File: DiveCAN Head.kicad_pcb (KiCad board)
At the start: 4 copper layers, 55 x 41.8 mm, 114 parts, among them J1 Cell 1, J10 SOLENOID OUT, J2 Cell 2, J3 Cell 3, J4 POWER CONNECTION, J5 SSC1, J6 SSC1, J7 SSC1, J8 Conn_01x05_Socket, J9 Conn_01x05_Socket, Q2 DMG1012T, U1 ATtiny102-SS, U10 AVR32EA28, U11 MCP2515-xSO, U12 TCAN330, U13 TPS63001, U15 74LVC2G14, U16 TPS63001, U2 TPS2115, U3 ATtiny102-SS, U4 TPS2115, U5 ATtiny102-SS, U6 TPS2115, U7 AVR32EA28, U8 MCP2515-xSO, U9 TCAN330

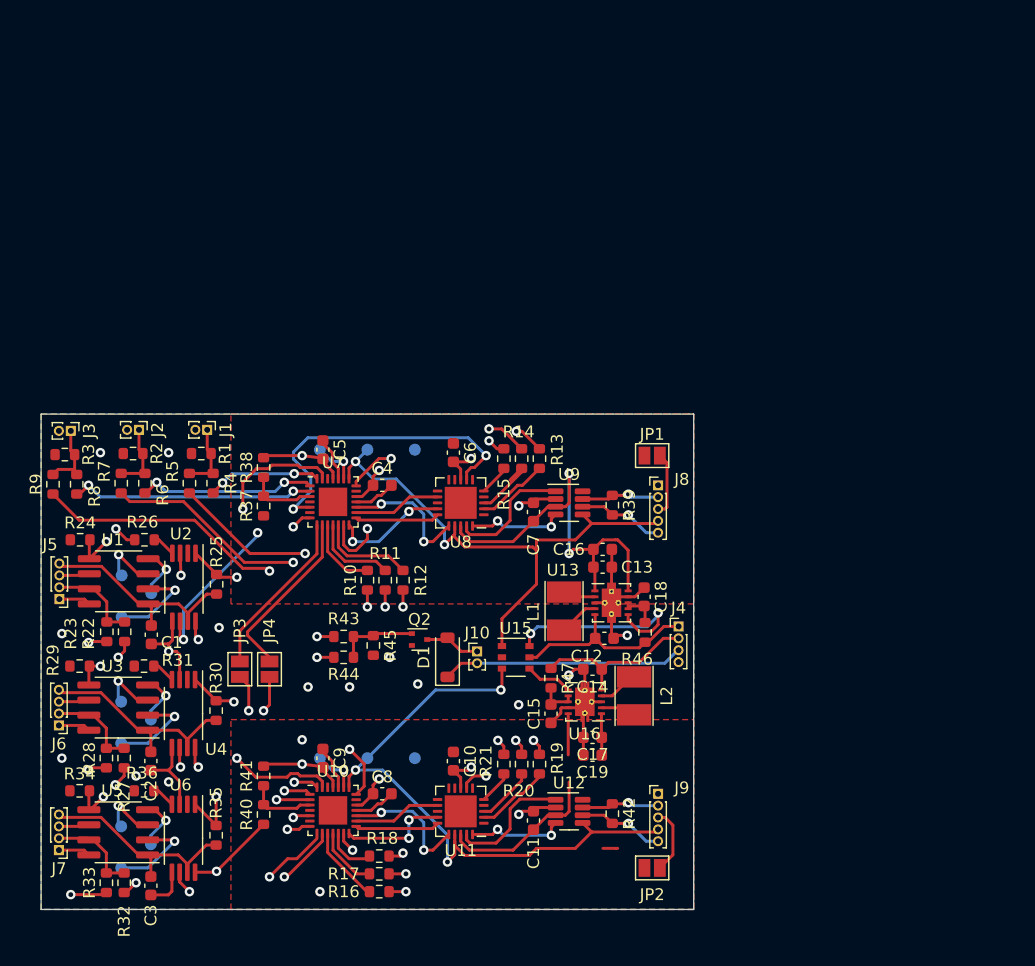
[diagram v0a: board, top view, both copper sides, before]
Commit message: 
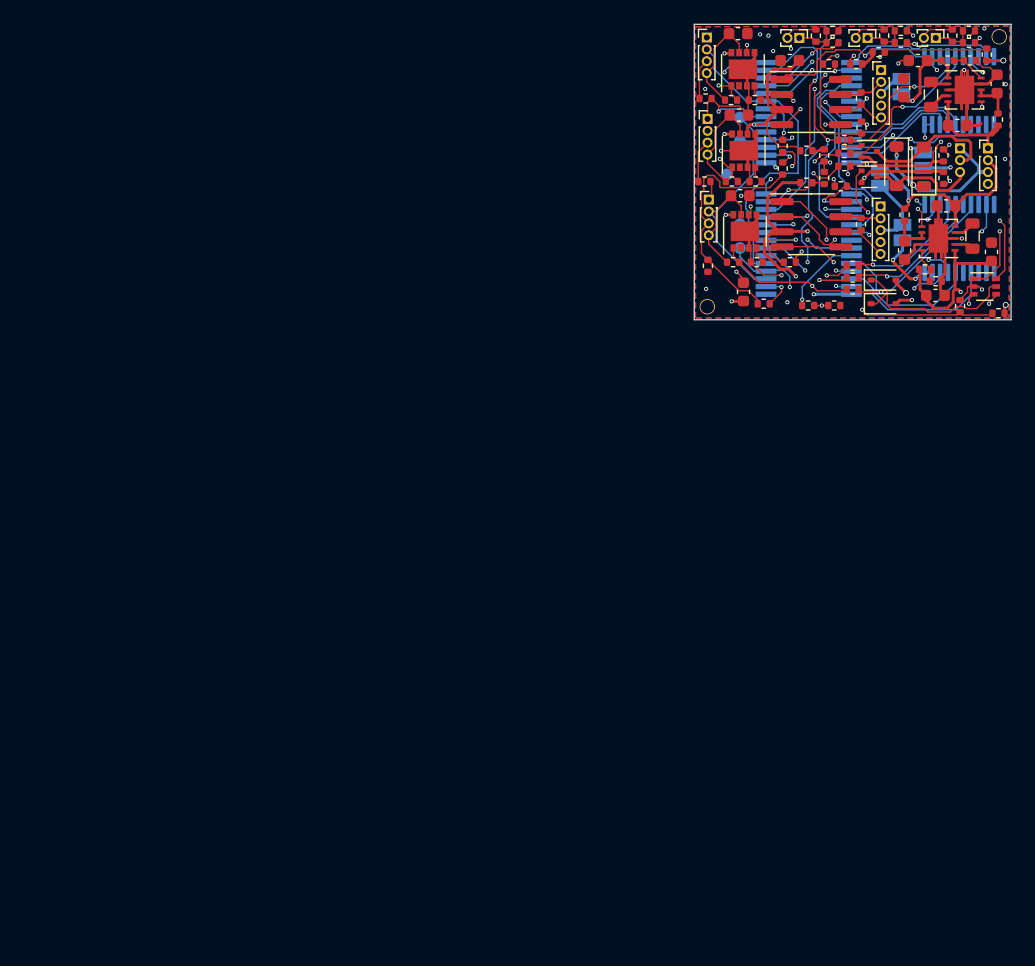
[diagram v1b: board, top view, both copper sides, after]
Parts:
- removed the C10 at (79.8, 154.2)
- removed the C11 at (86.5, 159.2)
- removed the C5 at (68.8, 128.0)
- removed the C6 at (79.8, 128.2)
- removed the C7 at (86.5, 133.2)
- removed the C9 at (68.8, 154.0)
- removed the J1 at (59.0, 126.3)
- removed the J3 at (47.5, 126.4)
- removed the R24 at (48.3, 135.6)
- removed the R27 at (52.0, 154.0)
- removed the R28 at (50.5, 154.0)
- removed the R29 at (48.2, 146.2)
- removed the R34 at (48.2, 156.8)
- removed the R4 at (59.5, 130.8)
- removed the R5 at (57.5, 130.8)
- removed the R6 at (53.8, 130.8)
- removed the R7 at (51.8, 130.8)
- removed the R8 at (48.0, 130.9)
- removed the R9 at (46.0, 130.9)
- removed TP12, TP15: GND, TestPoint:TestPoint_Pad_D1.0mm
- removed the TP2 at (51.8, 138.6)
- removed the TP3 at (51.8, 142.1)
- removed the TP4 at (54.2, 150.7)
- removed the TP5 at (51.8, 149.2)
- removed TP6, TP9: SSC_TPICLK, TestPoint:TestPoint_Pad_D1.0mm
- removed TP7: SSC_RST, TestPoint:TestPoint_Pad_D1.0mm
- removed TP8: SSC_TPIDATA, TestPoint:TestPoint_Pad_D1.0mm
- removed the U1 at (51.5, 139.1)
- removed the U3 at (51.5, 149.7)
- removed the U5 at (51.5, 160.2)
- added D1: 1N5819WS, Diode_SMD:D_SOD-323, F.Cu at (116.0, 113.7)
- added D2: 1N5819WS, Diode_SMD:D_SOD-323, F.Cu at (116.0, 115.7)
- added D3: MBR0520, Diode_SMD:D_SOD-123, F.Cu at (119.4, 104.2)
- added J8: C1, Library:PinHeader_1x02_P1.00mm_Vertical, F.Cu at (120.4, 93.3)
- added J9: C1, Library:PinHeader_1x02_P1.00mm_Vertical, F.Cu at (114.7, 93.3)
- added Q1: DMG1012T, Package_TO_SOT_SMD:SOT-523, F.Cu at (114.8, 102.8)
- added R12: 200, Resistor_SMD:R_0402_1005Metric, F.Cu at (114.2, 100.8)
- added R13: 1M, Resistor_SMD:R_0402_1005Metric, F.Cu at (113.7, 95.5)
- added R20: 0.5, Resistor_SMD:R_0402_1005Metric, F.Cu at (121.0, 103.2)
- added R21: 200, Resistor_SMD:R_0402_1005Metric, F.Cu at (109.7, 115.8)
- added R37: 4.02k, Resistor_SMD:R_0402_1005Metric, F.Cu at (122.5, 115.9)
- added R38: 499k, Resistor_SMD:R_0402_1005Metric, F.Cu at (125.7, 116.5)
- added R40: 10K, Resistor_SMD:R_0402_1005Metric, F.Cu at (121.8, 93.1)
- added R41: 10K, Resistor_SMD:R_0402_1005Metric, F.Cu at (123.2, 93.7)
- added R42: 10K, Resistor_SMD:R_0402_1005Metric, F.Cu at (123.2, 92.7)
- added R46: 10K, Resistor_SMD:R_0402_1005Metric, F.Cu at (110.3, 93.1)
- added R47: 10K, Resistor_SMD:R_0402_1005Metric, F.Cu at (111.7, 93.7)
- added R48: 10K, Resistor_SMD:R_0402_1005Metric, F.Cu at (111.7, 92.7)
- added R49: 1M, Resistor_SMD:R_0402_1005Metric, F.Cu at (119.5, 112.8)
- added R50: 178k, Resistor_SMD:R_0402_1005Metric, F.Cu at (120.4, 113.8)
- added R51: 1M, Resistor_SMD:R_0402_1005Metric, F.Cu at (121.4, 95.2)
- added R52: 178k, Resistor_SMD:R_0402_1005Metric, F.Cu at (123.3, 95.2)
- added REF**: ToolingHoleJLC, Library:ToolingHoleJLC, F.Cu at (101.2, 116.0)
- added REF**: ToolingHoleJLC, Library:ToolingHoleJLC, F.Cu at (125.8, 93.2)
- J10: value SOLENOID OUT -> C1; footprint Connector_PinHeader_1.00mm:PinHeader_1x02_P1.00mm_Vertical -> Library:PinHeader_1x02_P1.00mm_Vertical
- J2: value Cell 2 -> Solenoid out; footprint Connector_PinHeader_1.00mm:PinHeader_1x02_P1.00mm_Vertical -> Connector_PinHeader_1.00mm:PinHeader_1x03_P1.00mm_Vertical; moved to B.Cu
- JP1, JP2, JP3, JP4: moved to B.Cu
- L1: renamed from L2; footprint Inductor_SMD:L_Taiyo-Yuden_NR-30xx_HandSoldering -> Inductor_SMD:L_0805_2012Metric
- L2: renamed from L1; footprint Inductor_SMD:L_Taiyo-Yuden_NR-30xx_HandSoldering -> Inductor_SMD:L_0805_2012Metric
- R1, R2, R3: value 10K -> 100k; footprint Resistor_SMD:R_0603_1608Metric -> Resistor_SMD:R_0402_1005Metric
- R10: renamed from R14; footprint Resistor_SMD:R_0603_1608Metric -> Resistor_SMD:R_0402_1005Metric
- R11: renamed from R15; footprint Resistor_SMD:R_0603_1608Metric -> Resistor_SMD:R_0402_1005Metric
- R14: renamed from R16; footprint Resistor_SMD:R_0603_1608Metric -> Resistor_SMD:R_0402_1005Metric
- R15: renamed from R17; footprint Resistor_SMD:R_0603_1608Metric -> Resistor_SMD:R_0402_1005Metric
- R16: renamed from R18; footprint Resistor_SMD:R_0603_1608Metric -> Resistor_SMD:R_0402_1005Metric
- R17: renamed from R19; footprint Resistor_SMD:R_0603_1608Metric -> Resistor_SMD:R_0402_1005Metric
- R18: renamed from R20; footprint Resistor_SMD:R_0603_1608Metric -> Resistor_SMD:R_0402_1005Metric
- R19: renamed from R21; footprint Resistor_SMD:R_0603_1608Metric -> Resistor_SMD:R_0402_1005Metric
- R22: value 5K -> 1M; footprint Resistor_SMD:R_0603_1608Metric -> Resistor_SMD:R_0402_1005Metric
- R23: value 5K -> 0.5; footprint Resistor_SMD:R_0603_1608Metric -> Resistor_SMD:R_0402_1005Metric
- R24: renamed from R25; footprint Resistor_SMD:R_0603_1608Metric -> Resistor_SMD:R_0402_1005Metric
- R25: renamed from R26; footprint Resistor_SMD:R_0603_1608Metric -> Resistor_SMD:R_0402_1005Metric
- R26: renamed from R30; footprint Resistor_SMD:R_0603_1608Metric -> Resistor_SMD:R_0402_1005Metric
- R27: renamed from R31; footprint Resistor_SMD:R_0603_1608Metric -> Resistor_SMD:R_0402_1005Metric
- R28: renamed from R35; footprint Resistor_SMD:R_0603_1608Metric -> Resistor_SMD:R_0402_1005Metric
- R29: renamed from R36; footprint Resistor_SMD:R_0603_1608Metric -> Resistor_SMD:R_0402_1005Metric
- R30: renamed from R37; value R -> 100k; footprint Resistor_SMD:R_0603_1608Metric -> Resistor_SMD:R_0402_1005Metric
- R31: renamed from R38; value R -> 4k; footprint Resistor_SMD:R_0603_1608Metric -> Resistor_SMD:R_0402_1005Metric
- R32: value 5K -> 4.02k; footprint Resistor_SMD:R_0603_1608Metric -> Resistor_SMD:R_0402_1005Metric
- R33: value 5K -> 499k; footprint Resistor_SMD:R_0603_1608Metric -> Resistor_SMD:R_0402_1005Metric
- R34: renamed from R39; footprint Resistor_SMD:R_0603_1608Metric -> Resistor_SMD:R_0402_1005Metric
- R35: renamed from R40; value R -> 100k; footprint Resistor_SMD:R_0603_1608Metric -> Resistor_SMD:R_0402_1005Metric
- R36: renamed from R41; value R -> 4k; footprint Resistor_SMD:R_0603_1608Metric -> Resistor_SMD:R_0402_1005Metric
- R39: renamed from R42; footprint Resistor_SMD:R_0603_1608Metric -> Resistor_SMD:R_0402_1005Metric
- R4: renamed from R47; footprint Resistor_SMD:R_0603_1608Metric -> Resistor_SMD:R_0402_1005Metric
- R43, R44: value 5K -> 10K; footprint Resistor_SMD:R_0603_1608Metric -> Resistor_SMD:R_0402_1005Metric
- R45: value 20K -> 10K; footprint Resistor_SMD:R_0603_1608Metric -> Resistor_SMD:R_0402_1005Metric
- R5: renamed from R46; footprint Resistor_SMD:R_0603_1608Metric -> Resistor_SMD:R_0402_1005Metric
- R6: renamed from R10; footprint Resistor_SMD:R_0603_1608Metric -> Resistor_SMD:R_0402_1005Metric
- R7: renamed from R11; footprint Resistor_SMD:R_0603_1608Metric -> Resistor_SMD:R_0402_1005Metric
- R8: renamed from R12; footprint Resistor_SMD:R_0603_1608Metric -> Resistor_SMD:R_0402_1005Metric
- R9: renamed from R13; footprint Resistor_SMD:R_0603_1608Metric -> Resistor_SMD:R_0402_1005Metric
- TP1: value SSC_RST -> GND
- U1: renamed from U15; footprint Package_SO:TSOP-6_1.65x3.05mm_P0.95mm -> Package_TO_SOT_SMD:SOT-363_SC-70-6
- U10, U7: footprint Package_DFN_QFN:VQFN-28-1EP_4x4mm_P0.45mm_EP2.4x2.4mm -> Package_SO:SSOP-28_5.3x10.2mm_P0.65mm; moved to B.Cu
- U11, U8: footprint Package_DFN_QFN:QFN-20-1EP_4x4mm_P0.5mm_EP2.7x2.7mm -> Package_SO:TSSOP-20_4.4x6.5mm_P0.65mm; moved to B.Cu
- U12, U9: footprint Package_TO_SOT_SMD:SOT-23-8 -> Package_SO:SOIC-8_3.9x4.9mm_P1.27mm
- U2: renamed from U16; value TPS63001 -> TPS63000; footprint Package_SON:Texas_DRC0010J_ThermalVias -> Package_SON:Texas_DRC0010J
- U3: renamed from U13; value TPS63001 -> TPS63000; footprint Package_SON:Texas_DRC0010J_ThermalVias -> Package_SON:Texas_DRC0010J
- U4: renamed from U2; footprint Package_SO:TSSOP-8_4.4x3mm_P0.65mm -> Library:VSON-8_3.3x3.3mm_P0.65mm_NexFET
- U5: renamed from U4; footprint Package_SO:TSSOP-8_4.4x3mm_P0.65mm -> Library:VSON-8_3.3x3.3mm_P0.65mm_NexFET
- U6: footprint Package_SO:TSSOP-8_4.4x3mm_P0.65mm -> Library:VSON-8_3.3x3.3mm_P0.65mm_NexFET
- moved R33 101.9 mm to (124.7, 94.7), turned to -90 degrees
- moved R32 94.6 mm to (115.6, 94.5), turned to 180 degrees
- moved R23 80.2 mm to (121.0, 105.1), turned to -90 degrees
- moved J5 77.5 mm to (101.3, 106.9), turned to 0 degrees
- moved C11 76.5 mm to (103.9, 106.6), turned to 0 degrees
- moved J4 74.8 mm to (101.2, 100.1), turned to 0 degrees
- moved C10 73.6 mm to (103.8, 99.8), turned to 0 degrees
- moved J2 73.2 mm to (122.5, 102.6), turned to 180 degrees
- moved J3 72.2 mm to (101.1, 93.3), turned to 0 degrees
- moved JP3 71.8 mm to (119.3, 103.6), turned to 90 degrees
- moved C9 70.8 mm to (103.7, 92.9), turned to 0 degrees
- moved R35 70.2 mm to (109.5, 105.5), turned to 0 degrees
- moved R44 69.9 mm to (117.5, 93.7)
- moved R15 69.8 mm to (112.4, 105.8), turned to 0 degrees
- moved U6 69.7 mm to (104.3, 109.6), turned to 90 degrees
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- renumbered C14 to C1, C2 to C10, C3 to C11, C4 to C12, C8 to C13, C12 to C2, C15 to C3, C18 to C4, C17 to C5, C13 to C6, C19 to C7, C16 to C8, C1 to C9, D1 to D4, J4 to J1, J5 to J3, J6 to J4, J7 to J5, J8 to J6, J9 to J7, TP10 to TP2, TP11 to TP3, TP13 to TP4, TP14 to TP5
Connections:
- D4 pad 2: Net-(D1-A) -> Net-(D4-A)
- J10 pad 1: Net-(D1-A) -> Net-(J10-Pin_1)
- J10 pad 2: /BUS_SOLENOID -> GNDREF
- J2 pad 1: Net-(J2-Pin_1) -> /BUS_SOLENOID
- J2 pad 2: GNDREF -> Net-(D3-A)
- J3 pad 2: Net-(J5-Pin_2) -> /SSC1_TX
- J3 pad 3: Net-(J5-Pin_3) -> /SSC1_RX
- J4 pad 2: Net-(J6-Pin_2) (its old number) -> /SSC2_TX
- J4 pad 3: Net-(J6-Pin_3) -> /SSC2_RX
- J5 pad 2: Net-(J7-Pin_2) (its old number) -> /SSC3_TX
- J5 pad 3: Net-(J7-Pin_3) -> /SSC3_RX
- J6 pad 4: /EN_A -> /~{EN_A}
- J7 pad 4: /EN_B -> /~{EN_B}
- JP3 pad 1: /Controller A/SDA -> /IN_A
- JP3 pad 2: /Controller B/SDA -> /CAN_A_PWR
- JP4 pad 1: /Controller A/SCL -> /IN_B
- JP4 pad 2: /Controller B/SCL -> /CAN_B_PWR
- Q2 pad 2: GNDREF -> /Controller B/SOLENOID_RET
- Q2 pad 3: Net-(D1-A) -> Net-(D4-A)
- R1 pad 1: GNDREF -> /SSC1_RX
- R1 pad 2: Net-(J1-Pin_1) -> GNDREF
- R14 pad 1: /SSC1_OK -> /SSC1_RX
- R14 pad 2: /Controller B/SSC1_OK -> /Controller B/SSC1_RX
- R15 pad 1: /SSC2_OK -> /SSC2_RX
- R15 pad 2: /Controller B/SSC2_OK -> /Controller B/SSC2_RX
- R16 pad 1: /SSC3_OK -> /SSC3_RX
- R16 pad 2: /Controller B/SSC3_OK -> /Controller B/SSC3_RX
- R2 pad 1: GNDREF -> /SSC2_RX
- R2 pad 2: Net-(J2-Pin_1) -> GNDREF
- R22 pad 1: /SSC1_A -> Net-(Q2-G)
- R22 pad 2: Net-(J5-Pin_2) -> GNDREF
- R23 pad 1: /SSC1_B -> /Controller B/SOLENOID_RET
- R23 pad 2: Net-(J5-Pin_2) -> GNDREF
- R3 pad 1: GNDREF -> /SSC3_RX
- R3 pad 2: Net-(J3-Pin_1) -> GNDREF
- R32 pad 1: /SSC3_A -> Net-(U7-PD0)
- R32 pad 2: Net-(J7-Pin_2) (its old number) -> GNDREF
- R33 pad 1: /SSC3_B -> Net-(U7-PD0)
- R33 pad 2: Net-(J7-Pin_2) (its old number) -> /BUS_SOLENOID
- R43 pad 1: Net-(Q2-G) -> GNDREF
- R43 pad 2: /Controller A/SOLENOID -> Net-(J9-Pin_1)
- R44 pad 1: Net-(Q2-G) -> /C2_A
- R44 pad 2: /Controller B/SOLENOID -> Net-(J9-Pin_1)
- R45 pad 1: Net-(Q2-G) -> /C2_B
- R45 pad 2: GNDREF -> Net-(J9-Pin_1)
- R6 pad 1: /SSC1_OK -> /SSC1_RX
- R6 pad 2: /Controller A/SSC1_OK -> /Controller A/SSC1_RX
- R7 pad 1: /SSC2_OK -> /SSC2_RX
- R7 pad 2: /Controller A/SSC2_OK -> /Controller A/SSC2_RX
- R8 pad 1: /SSC3_OK -> /SSC3_RX
- R8 pad 2: /Controller A/SSC3_OK -> /Controller A/SSC3_RX
- TP1 pad 1: Net-(U1-~{RESET}/PA2) -> GNDREF
- TP2 pad 1: /EN_A -> /Controller A/RST
- TP4 pad 1: /EN_B -> /Controller B/RST
- U1 pad 1: /EN_A -> /~{EN_A}
- U1 pad 3: /EN_B -> /~{EN_B}
- U1 pad 5: /IN_A -> Net-(D1-K)
- U10 pad 1: /C2_B -> /Controller B/CLK
- U10 pad 10: /Controller B/SSC1_OK -> Net-(U10-PD4)
- U10 pad 11: /Controller B/SSC2_OK -> Net-(U10-PD5)
- U10 pad 12: /Controller B/SSC3_OK -> Net-(U10-PD6)
- U10 pad 13: /Controller B/SOLENOID -> Net-(U10-PD7)
- U10 pad 14: Net-(U10-PD4) -> /BUS_B
- U10 pad 15: Net-(U10-PD5) -> GNDREF
- U10 pad 16: Net-(U10-PD6) -> /Controller B/SSC3_RX
- U10 pad 17: Net-(U10-PD7) -> /SSC3_TX
- U10 pad 18: /BUS_B -> /Controller B/RST
- U10 pad 19: GNDREF -> /Controller B/UPDI
- U10 pad 2: /C3_B -> /Controller B/SSC2_RX
- U10 pad 20: unconnected-(U10-PF0_(XTAL32K1)-Pad20) -> /BUS_B
- U10 pad 21: /SSC3_B -> GNDREF
- U10 pad 22: /EN_B -> /Controller B/SSC1_RX
- U10 pad 23: /Controller B/UPDI -> /SSC1_TX
- U10 pad 24: /BUS_B -> /C1_B
- U10 pad 25: GNDREF -> /C2_B
- U10 pad 26: unconnected-(U10-PA0_(XTALHF1)-Pad26) -> /C3_B
- U10 pad 27: /SSC1_B -> Net-(U10-PA5)
- U10 pad 28: /C1_B -> /Controller B/SOLENOID_RET
- U10 pad 3: Net-(U10-PA5) -> /SSC2_TX
- U10 pad 4: unconnected-(U10-PA6-Pad4) -> /Controller A/SDA
- U10 pad 5: /Controller B/CLK -> /Controller A/SCL
- U10 pad 6: unconnected-(U10-PC0-Pad6) -> Net-(U10-PD0)
- U10 pad 7: /SSC2_B -> unconnected-(U10-PD1-Pad7)
- U10 pad 8: /Controller B/SDA -> /Controller A/RST
- U10 pad 9: /Controller B/SCL -> /Controller B/SOLENOID
- U11 pad 1: unconnected-(U11-CLKOUT/SOF-Pad1) -> Net-(U11-TXCAN)
- U11 pad 10: unconnected-(U11-~{RX0BF}-Pad10) -> GNDREF
- U11 pad 12: Net-(U10-PD6) -> unconnected-(U11-~{RX0BF}-Pad12)
- U11 pad 13: (no net) -> unconnected-(U11-~{INT}-Pad13)
- U11 pad 14: Net-(U10-PD4) -> Net-(U10-PD6)
- U11 pad 15: Net-(U10-PD5) -> (no net)
- U11 pad 16: Net-(U10-PD7) -> Net-(U10-PD4)
- U11 pad 17: /EN_B -> Net-(U10-PD5)
- U11 pad 18: /BUS_B -> Net-(U10-PD7)
- U11 pad 19: Net-(U11-TXCAN) -> /BUS_B
- U11 pad 2: /Controller B/SSC1_PWR -> Net-(U11-RXCAN)
- U11 pad 20: Net-(U11-RXCAN) -> /BUS_B
- U11 pad 3: /Controller B/SSC2_PWR -> unconnected-(U11-CLKOUT/SOF-Pad3)
- U11 pad 4: (no net) -> /Controller B/SSC1_PWR
- U11 pad 5: /Controller B/SSC3_PWR -> /Controller B/SSC2_PWR
- U11 pad 6: unconnected-(U11-OSC2-Pad6) -> (no net)
- U11 pad 7: /Controller B/CLK -> /Controller B/SSC3_PWR
- U11 pad 8: GNDREF -> unconnected-(U11-OSC2-Pad8)
- U11 pad 9: unconnected-(U11-~{RX1BF}-Pad9) -> /Controller B/CLK
- U12 pad 5: /EN_B -> GNDREF
- U2 pad 10: /BUS_B -> Net-(U2-FB)
- U3 pad 10: /BUS_A -> Net-(U3-FB)
- U7 pad 1: /C2_A -> /Controller A/CLK
- U7 pad 10: /Controller A/SSC1_OK -> Net-(U7-PD4)
- U7 pad 11: /Controller A/SSC2_OK -> Net-(U7-PD5)
- U7 pad 12: /Controller A/SSC3_OK -> Net-(U7-PD6)
- U7 pad 13: /Controller A/SOLENOID -> Net-(U7-PD7)
- U7 pad 14: Net-(U7-PD4) -> /BUS_A
- U7 pad 15: Net-(U7-PD5) -> GNDREF
- U7 pad 16: Net-(U7-PD6) -> /Controller A/SSC3_RX
- U7 pad 17: Net-(U7-PD7) -> /SSC3_TX
- U7 pad 18: /BUS_A -> /Controller A/RST
- U7 pad 19: GNDREF -> /Controller A/UPDI
- U7 pad 2: /C3_A -> /Controller A/SSC2_RX
- U7 pad 20: unconnected-(U7-PF0_(XTAL32K1)-Pad20) -> /BUS_A
- U7 pad 21: /SSC3_A -> GNDREF
- U7 pad 22: /EN_A -> /Controller A/SSC1_RX
- U7 pad 23: /Controller A/UPDI -> /SSC1_TX
- U7 pad 24: /BUS_A -> /C1_A
- U7 pad 25: GNDREF -> /C2_A
- U7 pad 26: unconnected-(U7-PA0_(XTALHF1)-Pad26) -> /C3_A
- U7 pad 27: /SSC1_A -> Net-(U7-PA5)
- U7 pad 28: /C1_A -> /Controller A/SOLENOID_RET
- U7 pad 3: Net-(U7-PA5) -> /SSC2_TX
- U7 pad 4: unconnected-(U7-PA6-Pad4) -> /Controller A/SDA
- U7 pad 5: /Controller A/CLK -> /Controller A/SCL
- U7 pad 6: unconnected-(U7-PC0-Pad6) -> Net-(U7-PD0)
- U7 pad 7: /SSC2_A -> unconnected-(U7-PD1-Pad7)
- U7 pad 8: /Controller A/SDA -> /Controller B/RST
- U7 pad 9: /Controller A/SCL -> /Controller A/SOLENOID
- U8 pad 1: unconnected-(U8-CLKOUT/SOF-Pad1) -> Net-(U8-TXCAN)
- U8 pad 10: unconnected-(U8-~{RX0BF}-Pad10) -> GNDREF
- U8 pad 12: Net-(U7-PD6) -> unconnected-(U8-~{RX0BF}-Pad12)
- U8 pad 13: (no net) -> unconnected-(U8-~{INT}-Pad13)
- U8 pad 14: Net-(U7-PD4) -> Net-(U7-PD6)
- U8 pad 15: Net-(U7-PD5) -> (no net)
- U8 pad 16: Net-(U7-PD7) -> Net-(U7-PD4)
- U8 pad 17: /EN_A -> Net-(U7-PD5)
- U8 pad 18: /BUS_A -> Net-(U7-PD7)
- U8 pad 19: Net-(U8-TXCAN) -> /BUS_A
- U8 pad 2: /Controller A/SSC1_PWR -> Net-(U8-RXCAN)
- U8 pad 20: Net-(U8-RXCAN) -> /BUS_A
- U8 pad 3: /Controller A/SSC2_PWR -> unconnected-(U8-CLKOUT/SOF-Pad3)
- U8 pad 4: (no net) -> /Controller A/SSC1_PWR
- U8 pad 5: /Controller A/SSC3_PWR -> /Controller A/SSC2_PWR
- U8 pad 6: unconnected-(U8-OSC2-Pad6) -> (no net)
- U8 pad 7: /Controller A/CLK -> /Controller A/SSC3_PWR
- U8 pad 8: GNDREF -> unconnected-(U8-OSC2-Pad8)
- U8 pad 9: unconnected-(U8-~{RX1BF}-Pad9) -> /Controller A/CLK
- U9 pad 5: /EN_A -> GNDREF
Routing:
- net /SSC3_A: track 60.0 -> 0.00 mm, vias 2 -> 0
- net /SSC1_OK: track 57.9 -> 0.00 mm, vias 3 -> 0
- net /SSC3_OK: track 54.3 -> 0.00 mm, vias 3 -> 0
- net /EN_B: track 53.3 -> 0.00 mm, vias 3 -> 0
- net /SSC2_OK: track 53.2 -> 0.00 mm, vias 4 -> 0
- net /EN_A: track 46.0 -> 0.00 mm, vias 2 -> 0
- net /SSC3_B: track 42.2 -> 0.00 mm, vias 3 -> 0
- net /Controller B/RST: track 0.00 -> 40.4 mm, vias 0 -> 3
- net /SSC3_PWR: track 60.5 -> 23.5 mm, vias 3 -> 2
- net /SSC2_A: track 36.2 -> 0.00 mm, vias 2 -> 0
- net /Controller A/SOLENOID_RET: track 0.00 -> 35.9 mm, vias 0 -> 2
- net /SSC2_PWR: track 61.2 -> 26.0 mm
- net /BUS_B: track 60.6 -> 94.9 mm, vias 3 -> 10
- net /SSC1_PWR: track 66.1 -> 32.3 mm, vias 3 -> 5
- net /SSC1_A: track 31.9 -> 0.00 mm, vias 2 -> 0
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- removed copper zone on F.Cu, net /BUS_A
- removed copper zone on F.Cu, net /BUS_B
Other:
- board size 55 x 41.8 mm -> 26.7 x 24.9 mm
- board text added: "C1"
- board text added: "C1+"
- board text added: "C2"
- board text added: "C2+"
- board text added: "C3"
- board text added: "C3+"
- board text added: "CBA"
- board text added: "CBB"
- board text added: "CIA"
- board text added: "CIB"
- board text added: "G"
- board text added: "JLCJLCJLCJLC"
- board text added: "R"
- board text added: "U"
